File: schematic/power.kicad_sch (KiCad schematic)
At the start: 12 parts, among them U2 TLV62569DBV

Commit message: Assign LCSC part numbers, mark PS1 DNP for JLC assembly
Every BOM line except PS1 now carries an LCSC field. Generic passives
move to JLC basic parts with equal or better ratings. Parts not stocked
at LCSC are swapped: C1/C2 to T520D227M010ATE018 (10 V), F1 to
0805L035/24XR, J8 to a generic gold 2x6 header, D6 to SMF3.3A.
PS1 (Ag9905MT) is DNP: bought separately and hand-soldered.
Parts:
- C1, C2: value 220u/6V3 Ta-poly -> 220u/10V Ta-poly; LCSC (none) -> C116742; MPN T520D227M006ATE015 -> T520D227M010ATE018
- C3, C4: LCSC (none) -> C45783; MPN CL21A226MAYNNNE -> CL21A226MAQNNNE
- D1: LCSC (none) -> C110521
- D2, D3: LCSC (none) -> C8678
- L1: LCSC (none) -> C43389
- PS1: now not fitted
- R1: LCSC (none) -> C25741; MANUFACTURER YAGEO -> UNI-ROYAL; MPN RC0402FR-07100KL -> 0402WGF1003TCE
- R2: LCSC (none) -> C163478
- U2: LCSC (none) -> C141836
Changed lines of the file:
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@@
+			)
+		)
+		(property "LCSC" "C110521"
+			(at 35.56 50.8 0)
+			(hide yes)
+			(show_name no)
+			(do_not_autoplace no)
+			(effects
+				(font
+					(size 1.27 1.27)
+				)
 			)
 		)
@@
 		(on_board yes)
 		(in_pos_files yes)
-		(dnp no)
+		(dnp yes)
 		(fields_autoplaced no)
 		(property "Reference" "PS1"
@@
 			)
 		)
-		(property "Value" "220u/6V3 Ta-poly"
+		(property "Value" "220u/10V Ta-poly"
 			(at 91.44 48.26 0)
 			(show_name no)
@@
 			)
 		)
-		(property "MPN" "T520D227M006ATE015"
+		(property "MPN" "T520D227M010ATE018"
+			(at 88.9 46.99 0)
+			(hide yes)
+			(show_name no)
+			(do_not_autoplace no)
+			(effects
+				(font
+					(size 1.27 1.27)
+				)
+			)
+		)
+		(property "LCSC" "C116742"
 			(at 88.9 46.99 0)
 			(hide yes)
@@
 			)
 		)
+		(property "LCSC" "C8678"
+			(at 121.92 43.18 0)
+			(hide yes)
+			(show_name no)
+			(do_not_autoplace no)
+			(effects
+				(font
+					(size 1.27 1.27)
+				)
+			)
+		)
 		(pin "1"
 		)
@@
 			)
 		)
+		(property "LCSC" "C8678"
+			(at 121.92 63.5 0)
+			(hide yes)
+			(show_name no)
+			(do_not_autoplace no)
+			(effects
+				(font
+					(size 1.27 1.27)
+				)
+			)
+		)
 		(pin "1"
 		)
@@
 			)
 		)
-		(property "Value" "220u/6V3 Ta-poly"
+		(property "Value" "220u/10V Ta-poly"
 			(at 139.7 48.26 0)
 			(show_name no)
@@
 			)
 		)
-		(property "MPN" "T520D227M006ATE015"
+		(property "MPN" "T520D227M010ATE018"
+			(at 137.16 46.99 0)
+			(hide yes)
+			(show_name no)
+			(do_not_autoplace no)
+			(effects
+				(font
+					(size 1.27 1.27)
+				)
+			)
+		)
+		(property "LCSC" "C116742"
 			(at 137.16 46.99 0)
 			(hide yes)
@@
 			)
 		)
-		(property "MPN" "CL21A226MAYNNNE"
+		(property "MPN" "CL21A226MAQNNNE"
+			(at 162.56 46.99 0)
+			(hide yes)
+			(show_name no)
+			(do_not_autoplace no)
+			(effects
+				(font
+					(size 1.27 1.27)
+				)
+			)
+		)
+		(property "LCSC" "C45783"
 			(at 162.56 46.99 0)
 			(hide yes)
@@
 			)
 		)
+		(property "LCSC" "C141836"
+			(at 198.12 50.8 0)
+			(hide yes)
+			(show_name no)
+			(do_not_autoplace no)
+			(effects
+				(font
+					(size 1.27 1.27)
+				)
+			)
+		)
 		(pin "1"
 		)
@@
 			)
 		)
+		(property "LCSC" "C43389"
+			(at 218.44 48.26 0)
+			(hide yes)
+			(show_name no)
+			(do_not_autoplace no)
+			(effects
+				(font
+					(size 1.27 1.27)
+				)
+			)
+		)
 		(pin "1"
 		)
@@
 			)
 		)
-		(property "MANUFACTURER" "YAGEO"
+		(property "MANUFACTURER" "UNI-ROYAL"
 			(at 236.22 55.88 0)
 			(hide yes)
@@
 			)
 		)
-		(property "MPN" "RC0402FR-07100KL"
+		(property "MPN" "0402WGF1003TCE"
+			(at 236.22 55.88 0)
+			(hide yes)
+			(show_name no)
+			(do_not_autoplace no)
+			(effects
+				(font
+					(size 1.27 1.27)
+				)
+			)
+		)
+		(property "LCSC" "C25741"
 			(at 236.22 55.88 0)
 			(hide yes)
@@
 			)
 		)
+		(property "LCSC" "C163478"
+			(at 236.22 66.04 0)
+			(hide yes)
+			(show_name no)
+			(do_not_autoplace no)
+			(effects
+				(font
+					(size 1.27 1.27)
+				)
+			)
+		)
 		(pin "1"
 		)
@@
 			)
 		)
-		(property "MPN" "CL21A226MAYNNNE"
+		(property "MPN" "CL21A226MAQNNNE"
 			(at 246.38 52.07 0)
 			(hide yes)
+			(show_name no)
+			(do_not_autoplace no)
+			(effects
+				(font
+					(size 1.27 1.27)
+				)
+			)
+		)
+		(property "LCSC" "C45783"
+			(at 246.38 52.07 0)
+			(hide yes)

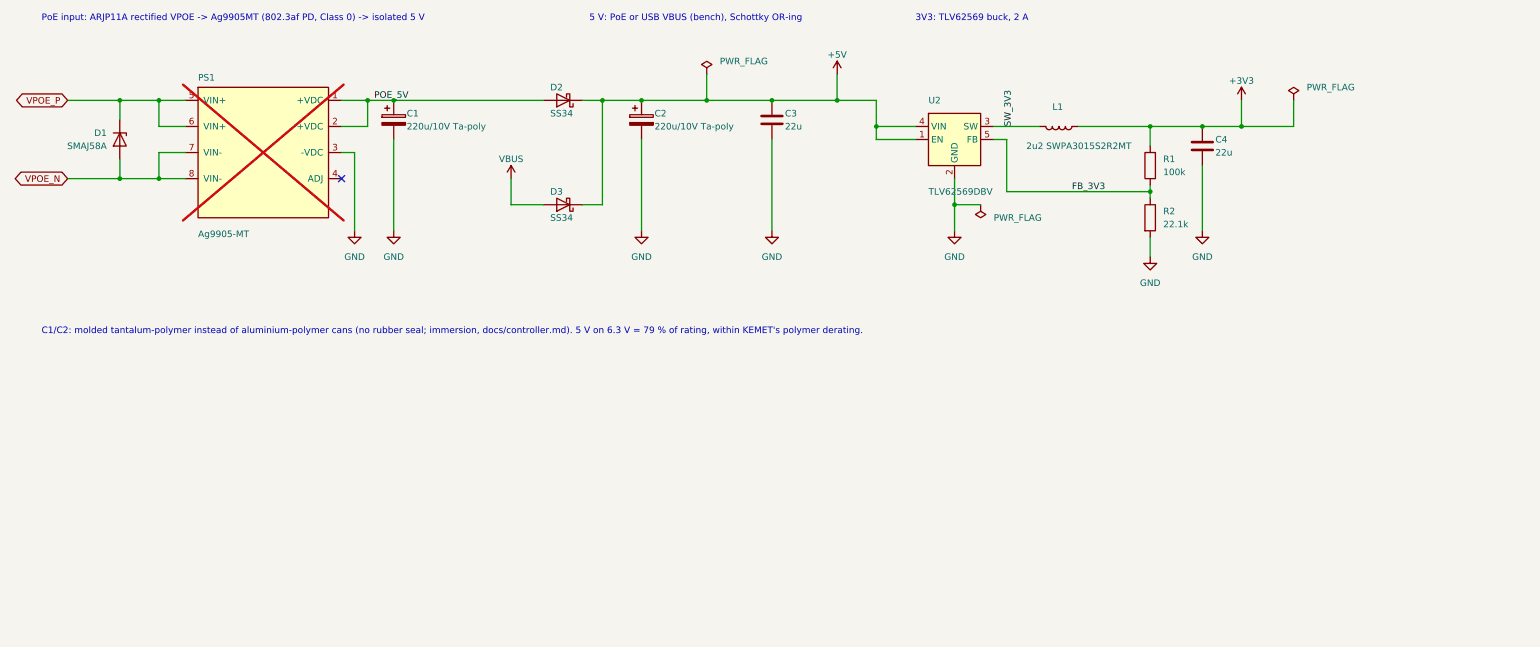
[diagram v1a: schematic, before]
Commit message: Power from the 19 V bus instead of PoE
Drop the Ag9905MT PoE module and the ARJP11A PoE magjack. New J3
(JST PH 2p) takes the frame's redundant 19 V bus: F3 PTC, D1 SMAJ22A
TVS, D8 SS34 reverse-polarity diode, U8 LMR51430 buck (1.1 MHz,
3.3 uH, 100k/13k -> 5.22 V) into the existing D2/D3 5 V OR-ing.
J1 becomes a HanRun HR911105A plain magjack (pin 8 Bob Smith to GND,
shield to ETH_SHLD). All new parts have LCSC numbers.

Net classes PWR_POE/PWR_POE_5V become PWR_19V/PWR_BUCK_5V; the PoE
clearance DRU rule is removed. Specs and handoff updated.
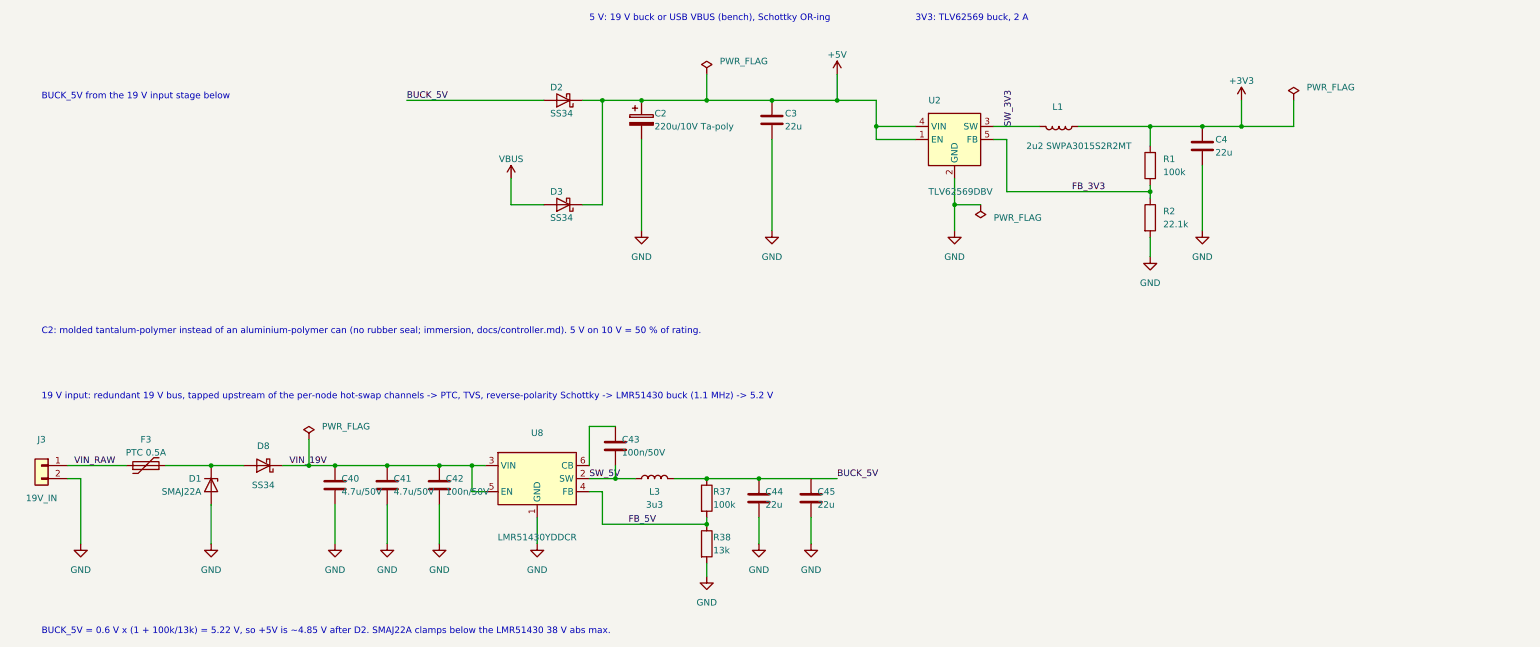
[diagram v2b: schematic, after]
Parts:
- removed C1: 220u/10V Ta-poly, Capacitor_Tantalum_SMD:CP_EIA-7343-31_Kemet-D, symbol Device:C_Polarized
- removed PS1: Ag9905-MT, granite:Silvertel_Ag9905MT, symbol granite:Ag9905M
- added C40, C41: 4.7u/50V, Capacitor_SMD:C_1206_3216Metric, symbol Device:C
- added C42, C43: 100n/50V, Capacitor_SMD:C_0402_1005Metric, symbol Device:C
- added C44, C45: 22u, Capacitor_SMD:C_0805_2012Metric, symbol Device:C
- added D8: SS34, Diode_SMD:D_SMA, symbol Device:D_Schottky
- added F3: PTC 0.5A, Fuse:Fuse_1206_3216Metric, symbol Device:Polyfuse
- added J3: 19V_IN, Connector_JST:JST_PH_B2B-PH-K_1x02_P2.00mm_Vertical, symbol Connector_Generic:Conn_01x02
- added L3: 3u3, Inductor_SMD:L_Changjiang_FXL0630, symbol Device:L
- added R37: 100k, Resistor_SMD:R_0402_1005Metric, symbol Device:R
- added R38: 13k, Resistor_SMD:R_0402_1005Metric, symbol Device:R
- added U8: LMR51430YDDCR, Package_TO_SOT_SMD:SOT-23-6, symbol Regulator_Switching:LMR51430
- D1: value SMAJ58A -> SMAJ22A; LCSC C110521 -> C41376403; MANUFACTURER Diodes Incorporated -> R+O; MPN SMAJ58A-13-F -> SMAJ22A
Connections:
- net VPOE_N is gone; now on net GND: D1.2 (A)
- net GND: now also C40.2, C41.2, C42.2, C44.2, C45.2, J3.2 (Pin_2), R38.2, U8.1 (GND)
- net POE_5V renamed BUCK_5V
- net BUCK_5V: now also C44.1, C45.1, L3.2, R37.1
- net VPOE_P: no longer names the net of D1.1 (K)
- net VPOE_P: now also D8.2 (A), F3.2
- new net: C43.1, U8.6 (CB)
- new net FB_5V: R37.2, R38.1, U8.4 (FB)
- new net SW_5V: C43.2, L3.1, U8.2 (SW)
- new net VIN_19V: C40.1, C41.1, C42.1, D8.1 (K), U8.3 (VIN), U8.5 (EN)
- new net VIN_RAW: F3.1, J3.1 (Pin_1)
- no-connect marks 1 -> 0
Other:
- note added: "19 V input: redundant 19 V bus, tapped upstream of the per-node hot-swap channels -> PTC, TVS, reverse-polarity Schottky -> LMR51430 buck (1.1 MHz) -> 5.2 V"
- note added: "5 V: 19 V buck or USB VBUS (bench), Schottky OR-ing"
- note added: "BUCK_5V = 0.6 V x (1 + 100k/13k) = 5.22 V, so +5V is ~4.85 V after D2. SMAJ22A clamps below the LMR51430 38 V abs max."
- note added: "BUCK_5V from the 19 V input stage below"
- note added: "C2: molded tantalum-polymer instead of an aluminium-polymer can (no rubber seal; immersion, docs/controller.md). 5 V on 10 V = 50 % of rating."
- note removed: "5 V: PoE or USB VBUS (bench), Schottky OR-ing"
- note removed: "C1/C2: molded tantalum-polymer instead of aluminium-polymer cans (no rubber seal; immersion, docs/controller.md). 5 V on 6.3 V = 79 % of rating, within KEMET's polymer derating."
- note removed: "PoE input: ARJP11A rectified VPOE -> Ag9905MT (802.3af PD, Class 0) -> isolated 5 V"

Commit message: WROOM-1-N8, node power sensing, dry contacts, I2C port, VIN sense
- U1 ESP32-C6-MINI-1-N4 -> ESP32-C6-WROOM-1-N8 (8 MB for two OTA
  slots; N16 is a drop-in). Project-local symbol and footprint from the
  datasheet. GPIO14 is not on the WROOM: EXP_nRESET_INT moves to
  GPIO10; GPIO11 spare.
- Node connectors J11-J18 go to JST PH 5p: PWR_SW, RST_SW, node GND,
  PLED+, PLED-. PLED drives 2x TLP290-4 AC-input optos; 10k pull-ups
  -> U15 MCP23017 @0x21 GPA0-7 (NODE_ON1-8).
- U15 GPB0-3: 4 dry-contact inputs (J10, RC + TPD4E05U06 ESD).
- J9 I2C sensor port (JST PH 4p, Qwiic order) on the protected header bus.
- VIN_SENSE 100k/10k divider to GPIO5 (ADC); J8 pin 9 now unused.
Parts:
- added C51: 100n, Capacitor_SMD:C_0402_1005Metric, symbol Device:C
- added R63: 100k, Resistor_SMD:R_0402_1005Metric, symbol Device:R
- added R64: 10k, Resistor_SMD:R_0402_1005Metric, symbol Device:R
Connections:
- net GND: now also C51.2, R64.2
- net VIN_19V: now also R63.1
- new net VIN_SENSE: C51.1, R63.2, R64.1
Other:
- note added: "VIN_SENSE = VIN_19V / 11 (100k/10k) -> ESP32 GPIO5 (ADC1). 19 V -> 1.73 V, 36 V clamp -> 3.27 V."

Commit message: Fix the 2026-10 review findings
Schematic: NODE_ON8 to U15 GPB4 (GPA7 is output-only), F3 1206L075/33NR,
VBUS bleeder R65/C52, R38 12.4k (BUCK_5V 5.44 V), D9 SMAJ6.0A crowbar on
BUCK_5V, R101-R116 270R, C26/C27 15 pF, R39-R46 47k, D6 value.

Layout: hole-clearance rule with units (0.3 mm) and 6.5 mm keep-outs at
H1-H4, EN RC / decoupling / VIN_SENSE filter at U1, no F.Cu under the
module body, vias kept off the U1 EPAD, zones 1 mm from the short edges
for mouse-bite rails, silk 1.0/0.15 mm, autorouter vias moved out of
SMD pads (only the U1 pad 29 thermal vias remain).

tools/jlcfab.py: per-footprint rotation/centroid corrections checked
against EasyEDA footprints (K*, U2, U8, JST fixed; U1, J2 offsets), no
drill maps in the zip. Docs: controller.md, handoff, review status.

ERC 0; DRC 0 unconnected, 0 parity, 3 known violations.
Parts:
- added C52: 2.2u/25V, Capacitor_SMD:C_0603_1608Metric, symbol Device:C
- added D9: SMAJ6.0A, Diode_SMD:D_SMA, symbol Device:D_Zener
- added R65: 4.7k, Resistor_SMD:R_0402_1005Metric, symbol Device:R
- F3: value PTC 0.5A -> PTC 0.75A; LCSC C19193043 -> C49196637; MPN 1206L050/33NR -> 1206L075/33NR
- R38: value 13k -> 12.4k 1%; LCSC C25754 -> C11692; MPN 0402WGF1302TCE -> 0402WGF1242TCE
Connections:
- net BUCK_5V: now also D9.1 (K)
- net GND: now also C52.2, D9.2 (A), R65.2
- net VBUS: now also C52.1, R65.1
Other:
- note added: "BUCK_5V = 0.6 V x (1 + 100k/12.4k) = 5.44 V, so +5V is ~5.0 V loaded after D2. D9 SMAJ6.0A crowbars BUCK_5V if U8 fails short (F3 trips). SMAJ22A clamps below the LMR51430 38 V abs max."
- note removed: "BUCK_5V = 0.6 V x (1 + 100k/13k) = 5.22 V, so +5V is ~4.85 V after D2. SMAJ22A clamps below the LMR51430 38 V abs max."
